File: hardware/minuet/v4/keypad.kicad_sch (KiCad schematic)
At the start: 3 parts, among them J10 G800LE300018YEU, J11 MTJ-889X1, J12 MTJ-669X1

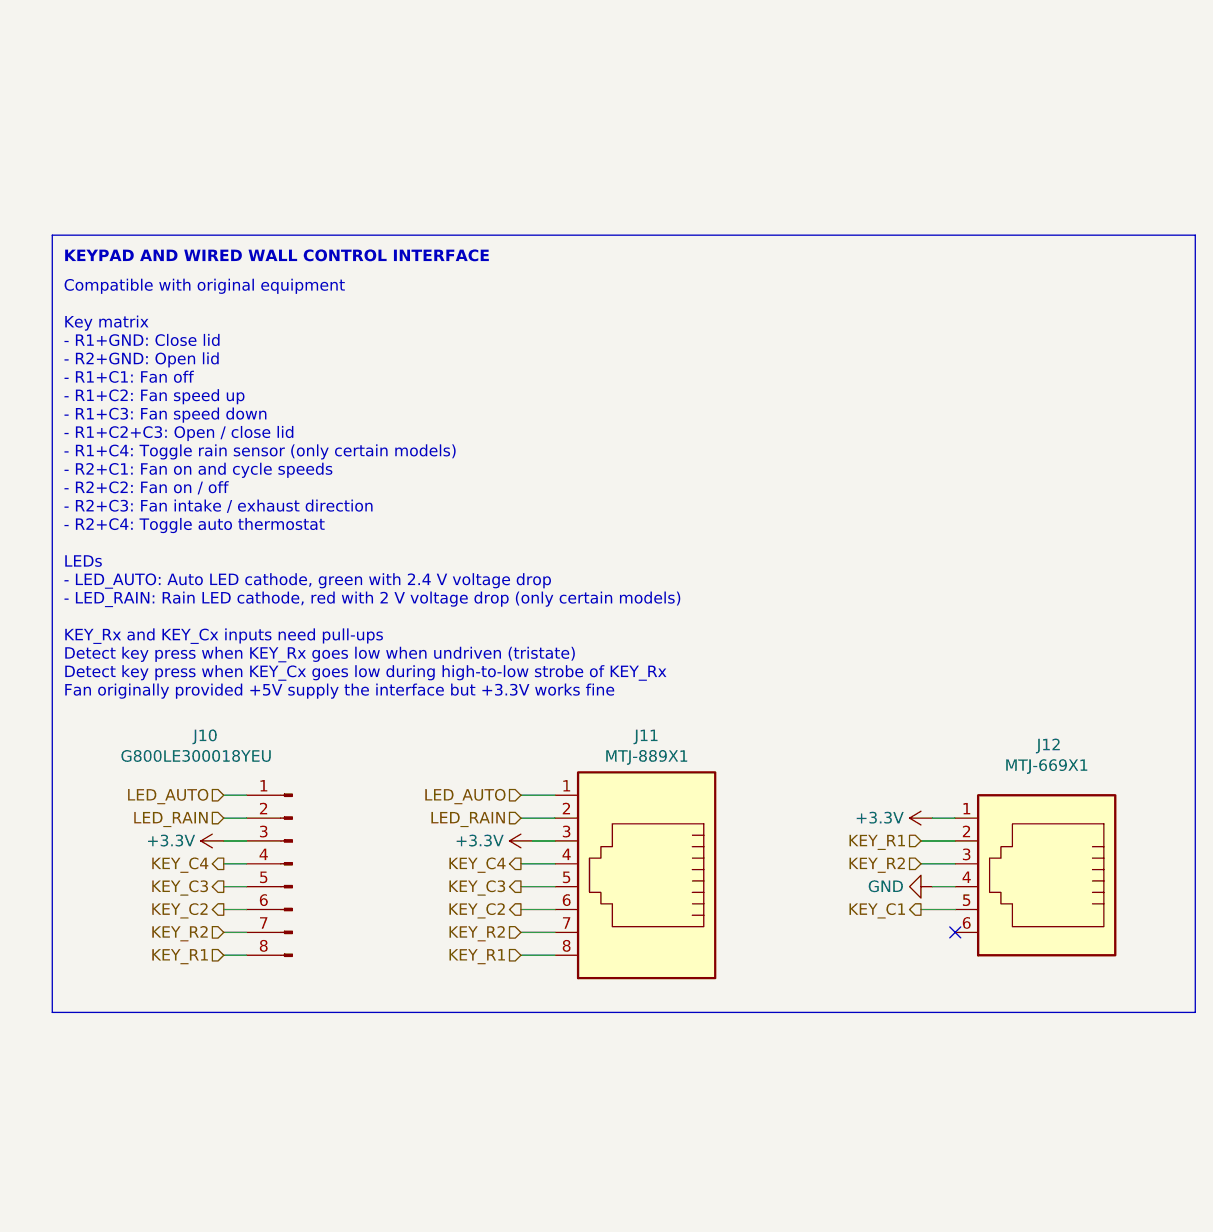
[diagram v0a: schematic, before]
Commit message: First draft of Minuet v4 fan controller board
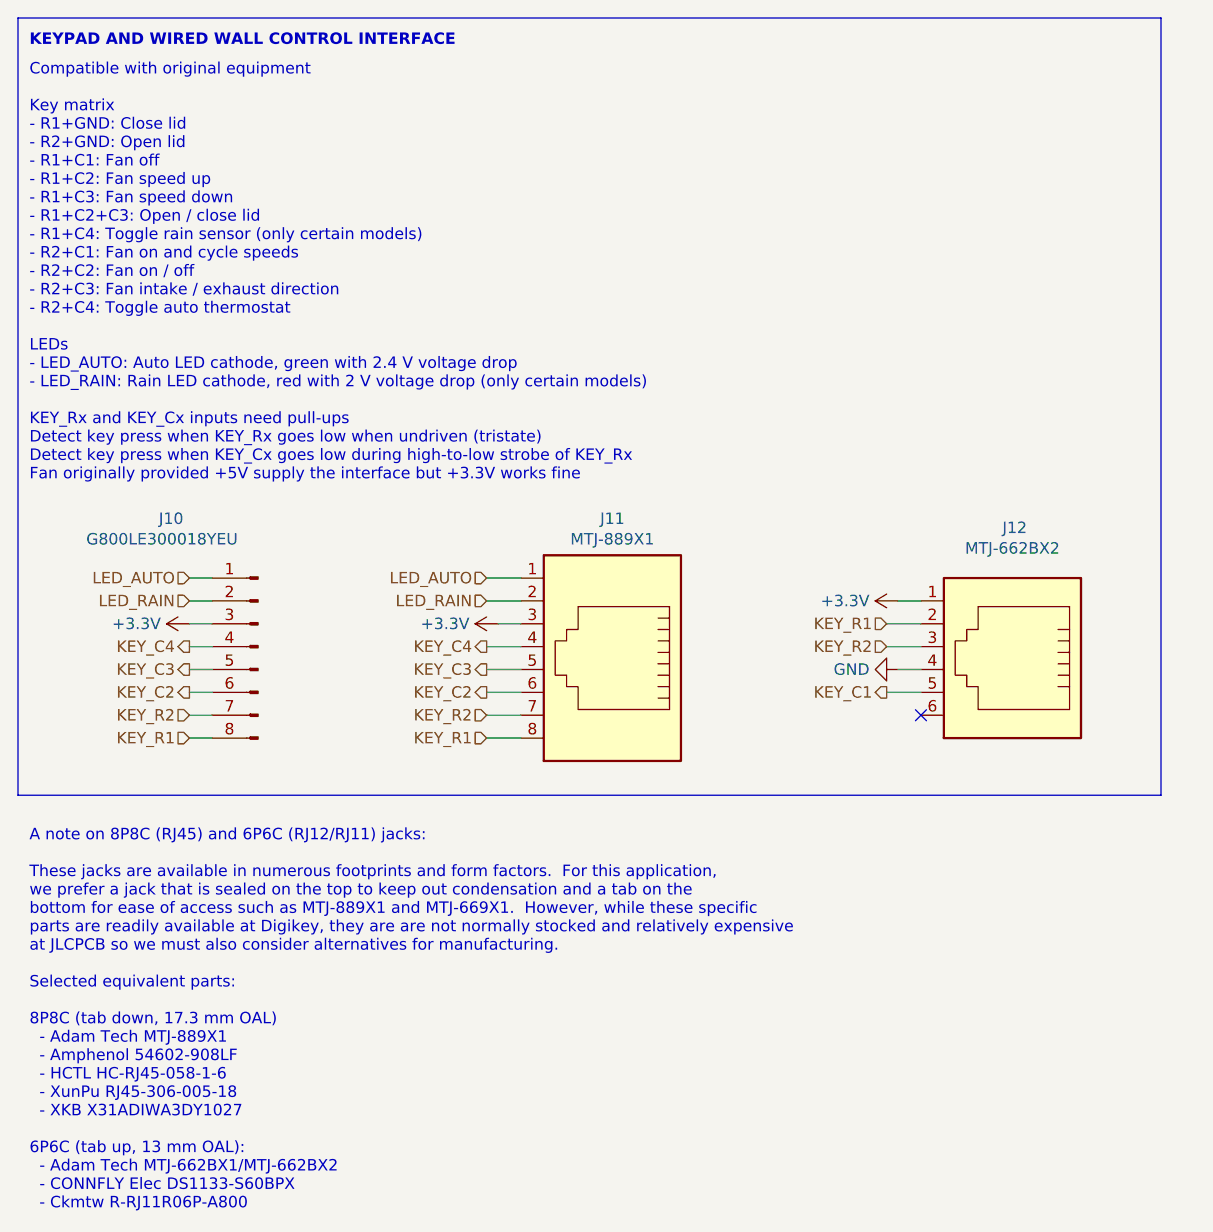
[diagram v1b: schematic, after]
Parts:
- J10: Alternative 0022284081 -> 22284081; LCSC_Preferred (none) -> C3345591
- J11: footprint MTJ-889X1:CONN_MTJ-889X1_ADM -> MTJ-889X1:MTJ-889X1; Alternative (none) -> HC-RJ45-058-1-6 (PBT); LCSC C6105889 -> C3000197; LCSC_Alternative (none) -> C3000197; LCSC_Preferred (none) -> C6105889
- J12: value MTJ-669X1 -> MTJ-662BX2; footprint MTJ-669X1:CONN_MTJ-669X1_ADM -> MTJ-662BX2:MTJ-662BX2; Alternate (none) -> DS1133-S60BPX; LCSC C5785037 -> C77859; LCSC_Alternate (none) -> C77859; LCSC_Preferred (none) -> C6105887
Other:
- note added: "A note on 8P8C (RJ45) and 6P6C (RJ12/RJ11) jacks: These jacks are available in numerous footprints and form factors. For this application, we prefer a jack that is sealed on the top to keep out condensation and a tab on the bottom for ease of access such as MTJ-889X1 and MTJ-669X1. However, while these specific parts are readily available at Digikey, they are are not normally stocked and relative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"
- company: (none) -> Brown Studios LLC
- moved on the sheet: J10, J11, J12

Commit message: Second draft of Minuet v4 main board.
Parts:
- J11: FT Position Offset (none) -> 0,3.5
- J12: Alternate DS1133-S60BPX -> (none); Alternative (none) -> DS1133-S60BPX; FT Position Offset (none) -> 0,1.35; FT Rotation Offset (none) -> 90; LCSC_Alternate C77859 -> (none); LCSC_Alternative (none) -> C77859
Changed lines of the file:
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@@
 		(dnp no)
 		(fields_autoplaced yes)
-		(property "Reference" "#PWR062"
+		(property "Reference" "#PWR064"
 			(at 113.03 97.79 0)
 			(effects
@@
 			(project "minuet"
 				(path "/5bd7983a-3caa-4bb2-9dc5-1af533f31e50/ecd3cea2-5b83-45e6-bc3a-38348e0ff880"
-					(reference "#PWR062")
+					(reference "#PWR064")
 					(unit 1)
 				)
@@
 			)
 		)
-		(property "LCSC_Alternate" "C77859"
-			(at 200.66 100.33 0)
-			(effects
-				(font
-					(size 1.27 1.27)
-				)
-				(hide yes)
-			)
-		)
-		(property "Alternate" "DS1133-S60BPX"
+		(property "LCSC_Alternative" "C77859"
+			(at 200.66 100.33 0)
+			(effects
+				(font
+					(size 1.27 1.27)
+				)
+				(hide yes)
+			)
+		)
+		(property "Alternative" "DS1133-S60BPX"
+			(at 200.66 100.33 0)
+			(effects
+				(font
+					(size 1.27 1.27)
+				)
+				(hide yes)
+			)
+		)
+		(property "FT Rotation Offset" "90"
+			(at 200.66 100.33 0)
+			(effects
+				(font
+					(size 1.27 1.27)
+				)
+				(hide yes)
+			)
+		)
+		(property "FT Position Offset" "0,1.35"
 			(at 200.66 100.33 0)
 			(effects
@@
 			)
 		)
+		(property "FT Position Offset" "0,3.5"
+			(at 156.21 100.33 0)
+			(effects
+				(font
+					(size 1.27 1.27)
+				)
+				(hide yes)
+			)
+		)
 		(pin "2"
 		)
@@
 		(dnp no)
 		(fields_autoplaced yes)
-		(property "Reference" "#PWR063"
+		(property "Reference" "#PWR065"
 			(at 147.32 97.79 0)
 			(effects
@@
 			(project "minuet"
 				(path "/5bd7983a-3caa-4bb2-9dc5-1af533f31e50/ecd3cea2-5b83-45e6-bc3a-38348e0ff880"
-					(reference "#PWR063")
+					(reference "#PWR065")
 					(unit 1)
 				)
@@
 		(dnp no)
 		(fields_autoplaced yes)
-		(property "Reference" "#PWR064"
+		(property "Reference" "#PWR066"
 			(at 181.61 102.87 0)
 			(effects
@@
 			(project "minuet"
 				(path "/5bd7983a-3caa-4bb2-9dc5-1af533f31e50/ecd3cea2-5b83-45e6-bc3a-38348e0ff880"
-					(reference "#PWR064")
+					(reference "#PWR066")
 					(unit 1)
 				)
@@
 		(dnp no)
 		(fields_autoplaced yes)
-		(property "Reference" "#PWR061"
+		(property "Reference" "#PWR063"
 			(at 191.77 95.25 0)
 			(effects
@@
 			(project "minuet"
 				(path "/5bd7983a-3caa-4bb2-9dc5-1af533f31e50/ecd3cea2-5b83-45e6-bc3a-38348e0ff880"
-					(reference "#PWR061")
+					(reference "#PWR063")
 					(unit 1)
 				)
